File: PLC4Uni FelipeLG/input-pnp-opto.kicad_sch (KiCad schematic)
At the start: 3 parts

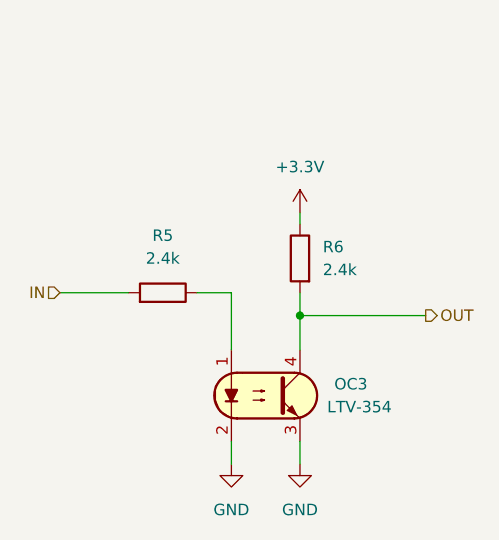
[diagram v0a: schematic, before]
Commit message: Add files via upload
Updated Circuitos corregidos y pistas agregadas
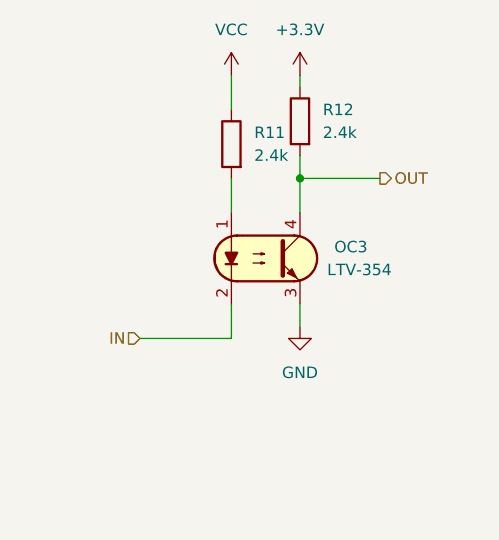
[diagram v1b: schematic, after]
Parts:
- removed R5, R6: 2.4k, Resistor_SMD_AKL:R_0603_1608Metric, symbol Resistor_AKL:R_0603
- added R11, R12: 2.4k, Resistor_SMD_AKL:R_0603_1608Metric, symbol Resistor_AKL:R_0603
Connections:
- net +3.3V: now also R12.2
- net GND: no longer OC3.2
- net IN: now also OC3.2
- net OUT: now also R12.1
- net at OC3.1: now also R11.1
- new net VCC: R11.2
